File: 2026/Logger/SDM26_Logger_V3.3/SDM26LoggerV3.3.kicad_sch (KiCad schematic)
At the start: 134 parts, among them IC1 ESP32-S3-WROOM-1-N8R8, IC2 CP2102N-A02-GQFN28, IC3 MIC37100-3.3WS, IC4 TPS563211DRLR, IC5 TLP175A_TPL,E, IC6 MIC37100-3.3WS, IC7 NEO-F9P-15B, IC8 TPS259250DRCR, J1 UART_USB, J2 ESP_USB, J3 GNSS_Debug, J4 Molex_1040310811, J5 1-776087-4, J6 1-776087-4, Q1 MMBT2222LT1G, Q2 MMBT2222LT1G, U1 INA260, U10 EMIF06-MSD02N16, U2 USBLC6-2SC6, U3 TPS2116DRL, U4 USBLC6-2SC6, U5 USBLC6-2SC6, U6 TPS2116, U7 SN65HVD230, U8 ADR425BRZ, U9 ADC128S102, Y1 ECX-.327-CDX-2096

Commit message: BSPD Formatting and misc
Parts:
- D1: symbol SDM_DIODES:ESDCAN03-2BWY -> SDM_ESD:ESDCAN03-2BWY

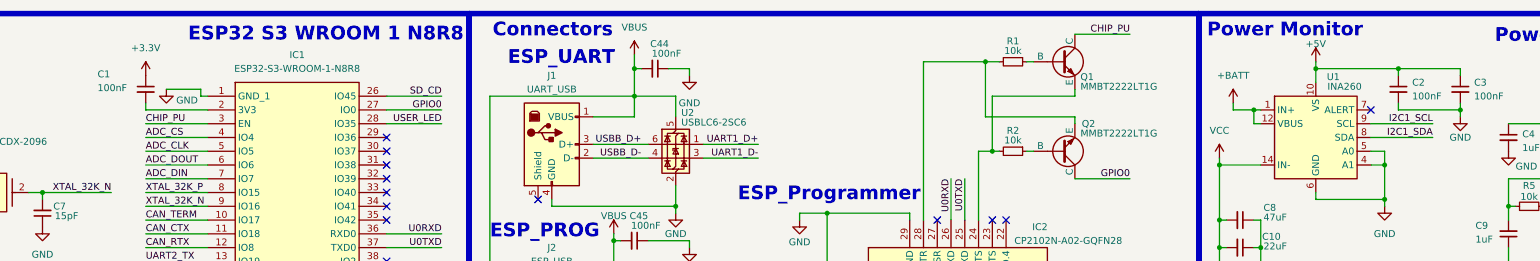
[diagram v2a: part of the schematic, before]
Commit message: Fixed decoupling capacitor on ESP32
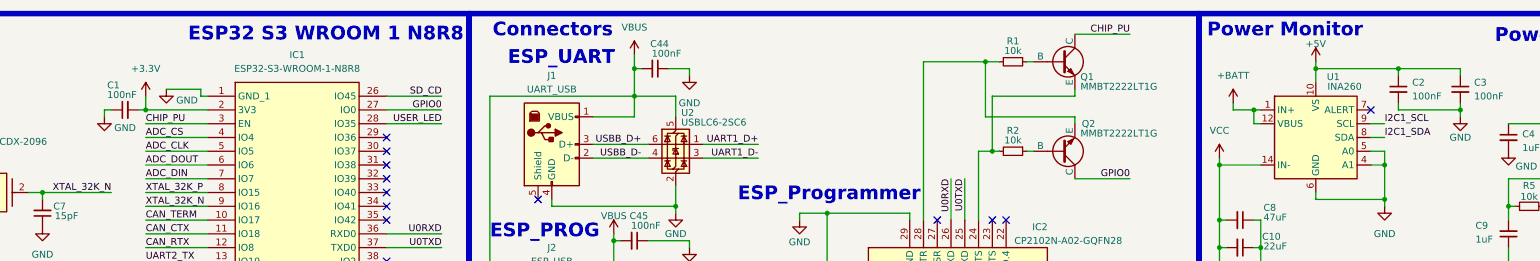
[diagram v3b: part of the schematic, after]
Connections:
- net +3.3V: now also C1.2, IC1.2 (3V3); no longer C1.1
- net GND: now also C1.1
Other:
- moved on the sheet: C1

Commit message: Logger 4.0 commit
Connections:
- net +3.3V: no longer IC1.2 (3V3)
- net GND: no longer C1.1
- new net: C1.1, IC1.2 (3V3)
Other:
- moved on the sheet: C1
